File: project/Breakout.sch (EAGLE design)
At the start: 47 parts, among them J1 I2C1, J2 I2C2, J3 ER-TFT1.28-1, U1 SY8088, U15 ETA1611, U4 ESP32-S3-WROOM-1

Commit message: Layout complete
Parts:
- B1: value (none) -> RESET
- B2: value (none) -> BOOT
- C105: value 10uF/16V -> 2.2uF/16V
- C106: value 10uF/16V -> 4.7uF/16V
- D19: value 1A/23V/620mV -> (none); device SparkFun-DiscreteSemi:DIODE-SCHOTTKY-BAT20J -> adafruit:DIODESOD-523
- R126: value 10 -> 6.6
- U15: value ETA1611 -> BD60A60NUX; device discrete:ETA1611 -> discrete:BD60A60NUX
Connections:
- removed net LCD_CTRL: R127.1
- removed net N$1 (its old number): C107.1, R127.2, U15.EN
- new net GPIO45: R127.1, U4.IO45
- new net LED_DIM: C107.1, R127.2, U15.PWM
- new net N$9: R126.2, U15.ISET
- net GPIO48: now also U15.EN
- net LED_A: now also U15.VOUT
- net LED_K: no longer R126.2
- net USB_5V: now also U15.VIN; no longer U15.IN
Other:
- moved on the sheet: C105, C106, C107, L6, R126, R127

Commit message: cleanup and fixes
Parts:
- removed C107: 22pF/50V, rcl:C-EUC0402
- removed R127: 10, rcl:R-US_R0402
- removed TP2: TEST-POINT3, SparkFun-Connectors:TEST-POINT3
- added C97: 0.1uF/6.3V, rcl:C-USC0402
- added C98: 4.7uF/6.3V, rcl:C-USC0402
- B1, B2: LCSC (none) -> C115362
- C1: LCSC (none) -> C106203
- C105: LCSC (none) -> C106853
- C106: LCSC (none) -> C277476
- C17, C2, C5: LCSC (none) -> C86275
- C18, C3, C4: LCSC (none) -> C161163
- C19: LCSC (none) -> C77007
- C86: value (none) -> 0.1uF/6.3V; device rcl:C-EUC0402 -> rcl:C-USC0402; LCSC (none) -> C541406
- CN2: LCSC (none) -> C64658
- D1, D15: LCSC (none) -> C511872
- D10, D8, D9: LCSC (none) -> C383211
- D11, D12, D2: LCSC (none) -> C172409
- D19: LCSC (none) -> C253516
- D3: LCSC (none) -> C375534
- J1, J2: LCSC (none) -> C495539
- L1: LCSC (none) -> C370436
- L6: LCSC (none) -> C518881
- R1, R13: LCSC (none) -> C60490
- R111, R112: LCSC (none) -> C106227
- R12, R123: LCSC (none) -> C100044
- R126: value 6.6 -> 20K; LCSC (none) -> C326980
- R2: LCSC (none) -> C163456
- R3: LCSC (none) -> C93947
- R74: LCSC (none) -> C163499
- TP1: value TEST-POINT3 -> TPTP06R; device SparkFun-Connectors:TEST-POINT3 -> testpad:TPTP06R
- U1: LCSC (none) -> C79313
- U15: LCSC (none) -> C2678724
- X1: LCSC (none) -> C40946
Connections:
- removed net LED_DIM: C107.1, R127.2, U15.PWM
- net GND: now also B1.2, B2.2, C97.2, C98.2; no longer C107.2, TP2.1
- net GPIO0: now also B2.3
- net GPIO45: now also U15.PWM; no longer R127.1
- net LED_K: now also TP1.TP
- net MCU_RST: now also B1.3
- net MCU_VDD: now also C97.1, C98.1, U15.VIN; no longer TP1.1
- net USB_5V: no longer U15.VIN
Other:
- moved on the sheet: B1, B2, C1, C105, C106, C17, C18, C19, C2, C3, C4, C5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

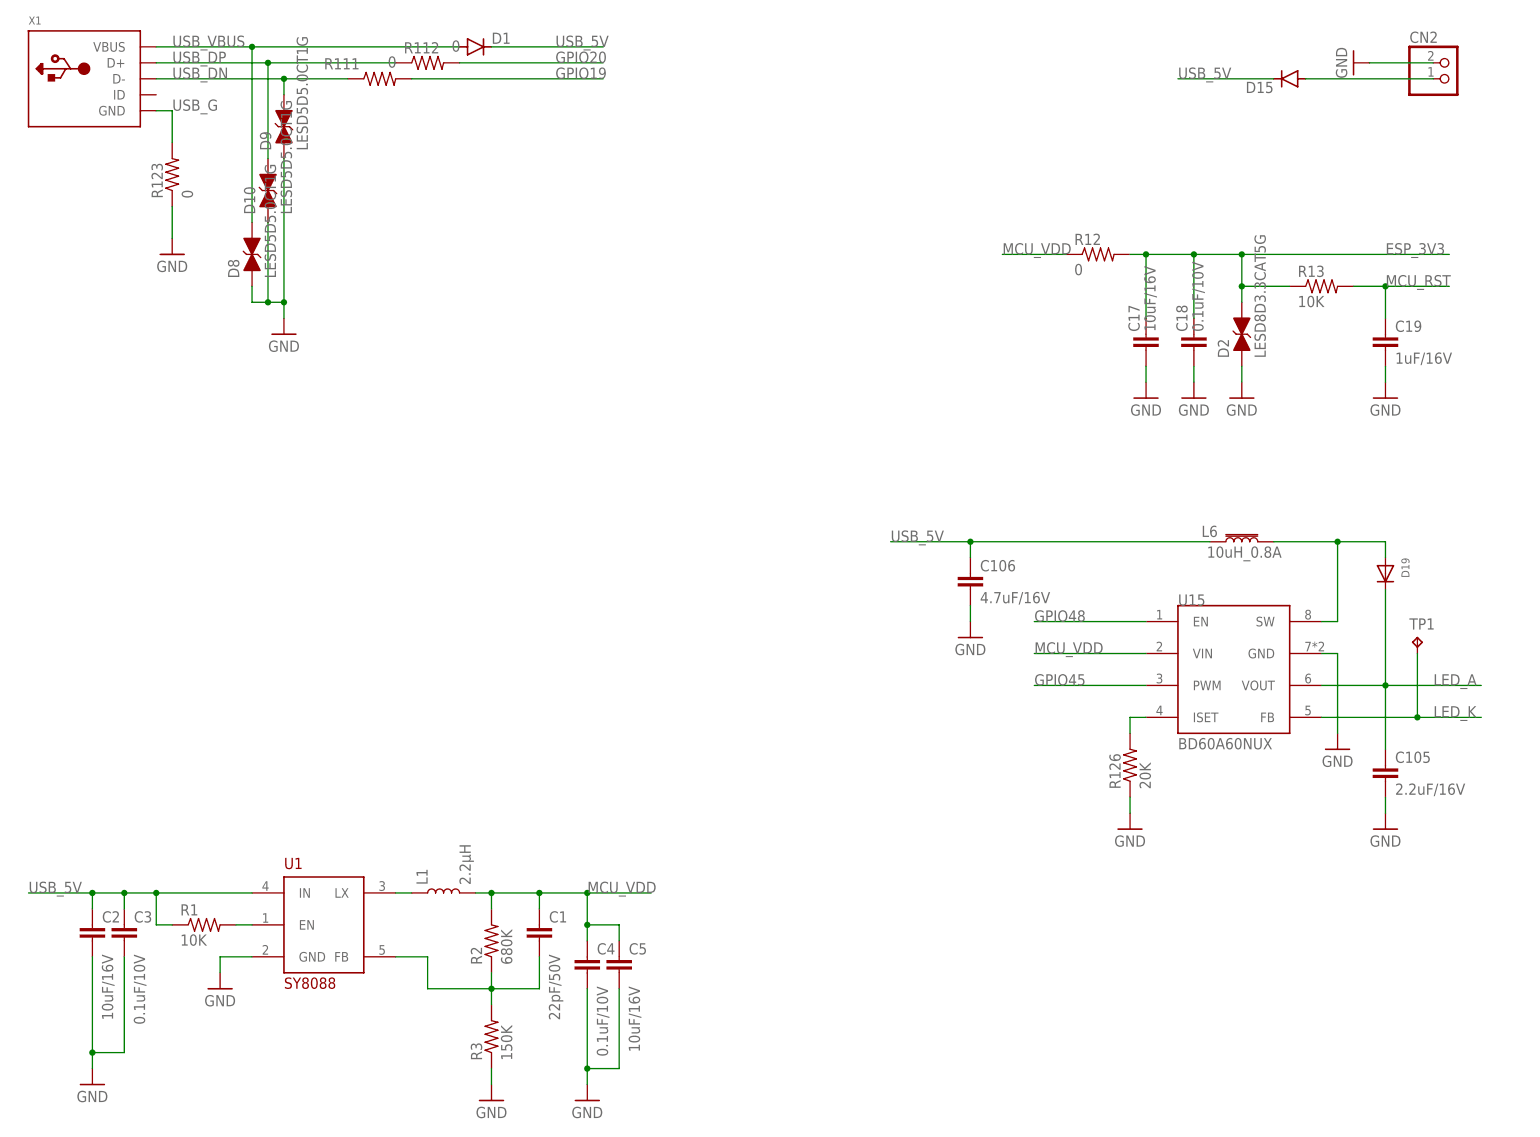
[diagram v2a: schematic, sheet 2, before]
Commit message: Display pinout fix
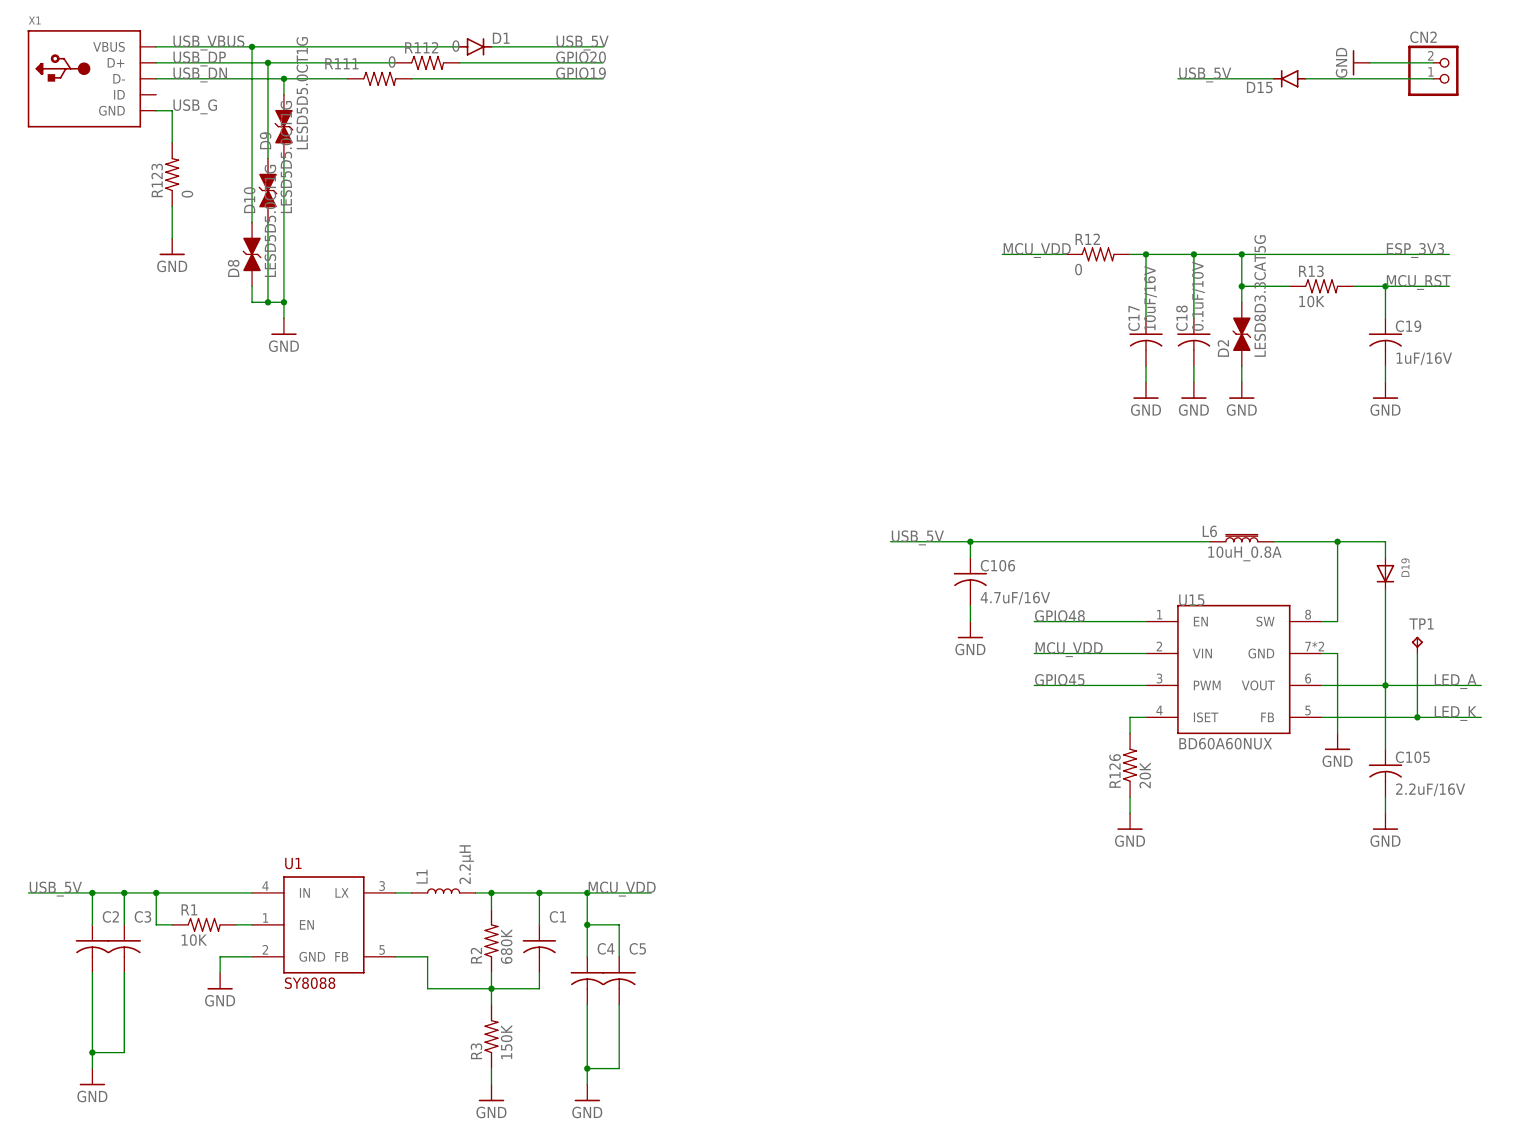
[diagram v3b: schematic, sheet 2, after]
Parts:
- added R14, R15: 4.7K, rcl:R-US_R0201
- added R16, R17: 1K, rcl:R-US_R0201
- C1: device SparkFun-Capacitors:22PF-0402T-16V-10% -> rcl:C-USC0402
- C105, C106, C17: device rcl:C-EUC0603 -> rcl:C-USC0603
- C18, C19: device rcl:C-EUC0402 -> rcl:C-USC0402
- C2: device SparkFun-Capacitors:10UF-0603-6.3V-20% -> rcl:C-USC0603
- C3: device SparkFun-Capacitors:0.1UF-0402-10V-10%-X7R -> rcl:C-USC0603
- C4: device SparkFun-Capacitors:0.1UF-0402-10V-10%-X7R -> rcl:C-USC0402
- C5: device SparkFun-Capacitors:10UF-0603-6.3V-20% -> rcl:C-USC0402
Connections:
- net GPIO18: now also R17.2
- net GPIO40: now also R14.2
- net GPIO41: now also R15.2
- net GPIO6: now also J3.SDA; no longer J3.SCL
- net GPIO7: now also J3.SCL; no longer J3.SDA
- net GPIO8: now also R16.2
- net MCU_VDD: now also R14.1, R15.1, R16.1, R17.1
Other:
- moved on the sheet: C1, C2, C3, C4, C5
